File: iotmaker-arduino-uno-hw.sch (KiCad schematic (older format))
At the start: 52 parts, among them J1 BARREL_JACK, J2 USB_A, J3 header Analog, J4 Header I2C, J5 Header module, J6 CONN_02X03, Q1 SI2301DS_GSD, SW1 RESET, SW2 SW_PUSH, U1 CH340G, U2 ATMEGA328P-AU, U3 LM358, U4 FAN1117A-3.3v, U5 FAN1117A-5.0v, Y1 16MHz_GND24, Y2 12MHz_GND24

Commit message: basic completed pcb
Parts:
- added J7: Header Analog, Pin_Headers:Pin_Header_Straight_1x05_Pitch2.54mm, symbol CONN_01X05
- added J8: DHT, Pin_Headers:Pin_Header_Straight_1x03_Pitch2.54mm, symbol CONN_01X03
- J3: value header Analog -> Servo
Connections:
- net +5V: now also J7.1 (P1), J7.4 (P4), J8.1 (P1)
- net ADC6: now also J5.4 (P4); no longer J3.3 (P3)
- net ADC7: now also J7.3 (P3); no longer J5.4 (P4)
- net GND: now also J7.2 (P2), J7.5 (P5), J8.3 (P3)
- net PB1: now also J3.3 (P3)
- net PD2: now also J8.2 (P2); no longer J5.3 (P3)
- net PD4: now also J5.3 (P3)
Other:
- moved on the sheet: J3, J4, J5

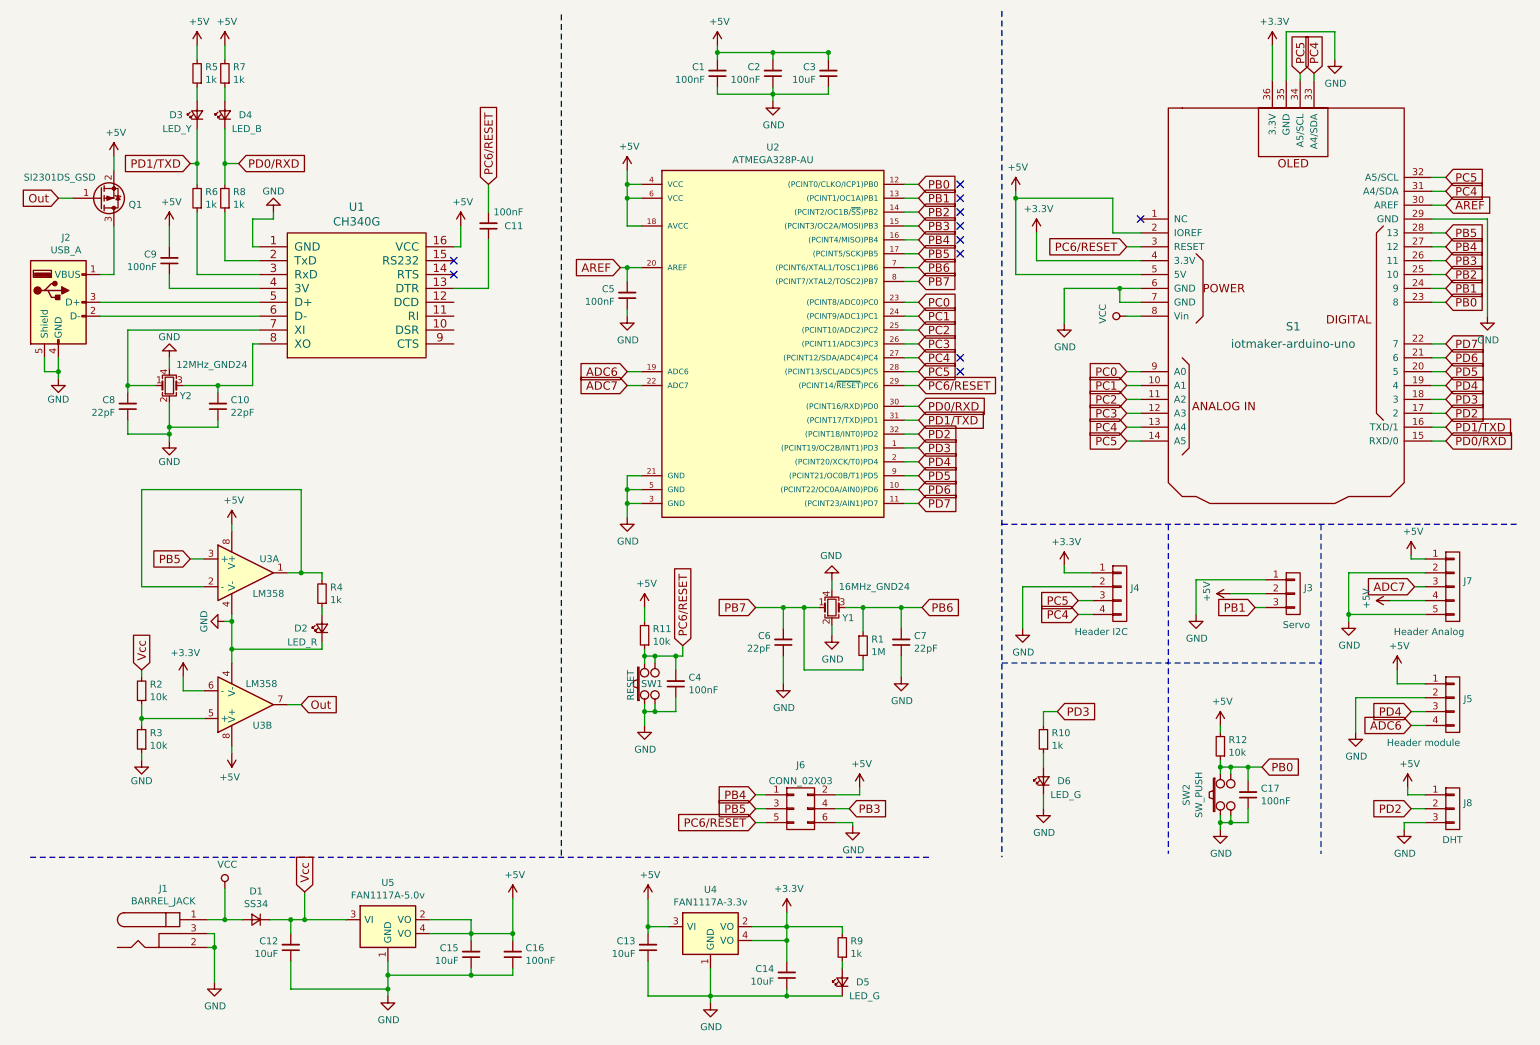
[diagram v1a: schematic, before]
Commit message: cchange CH340G to CH340E & update information board, gerber file
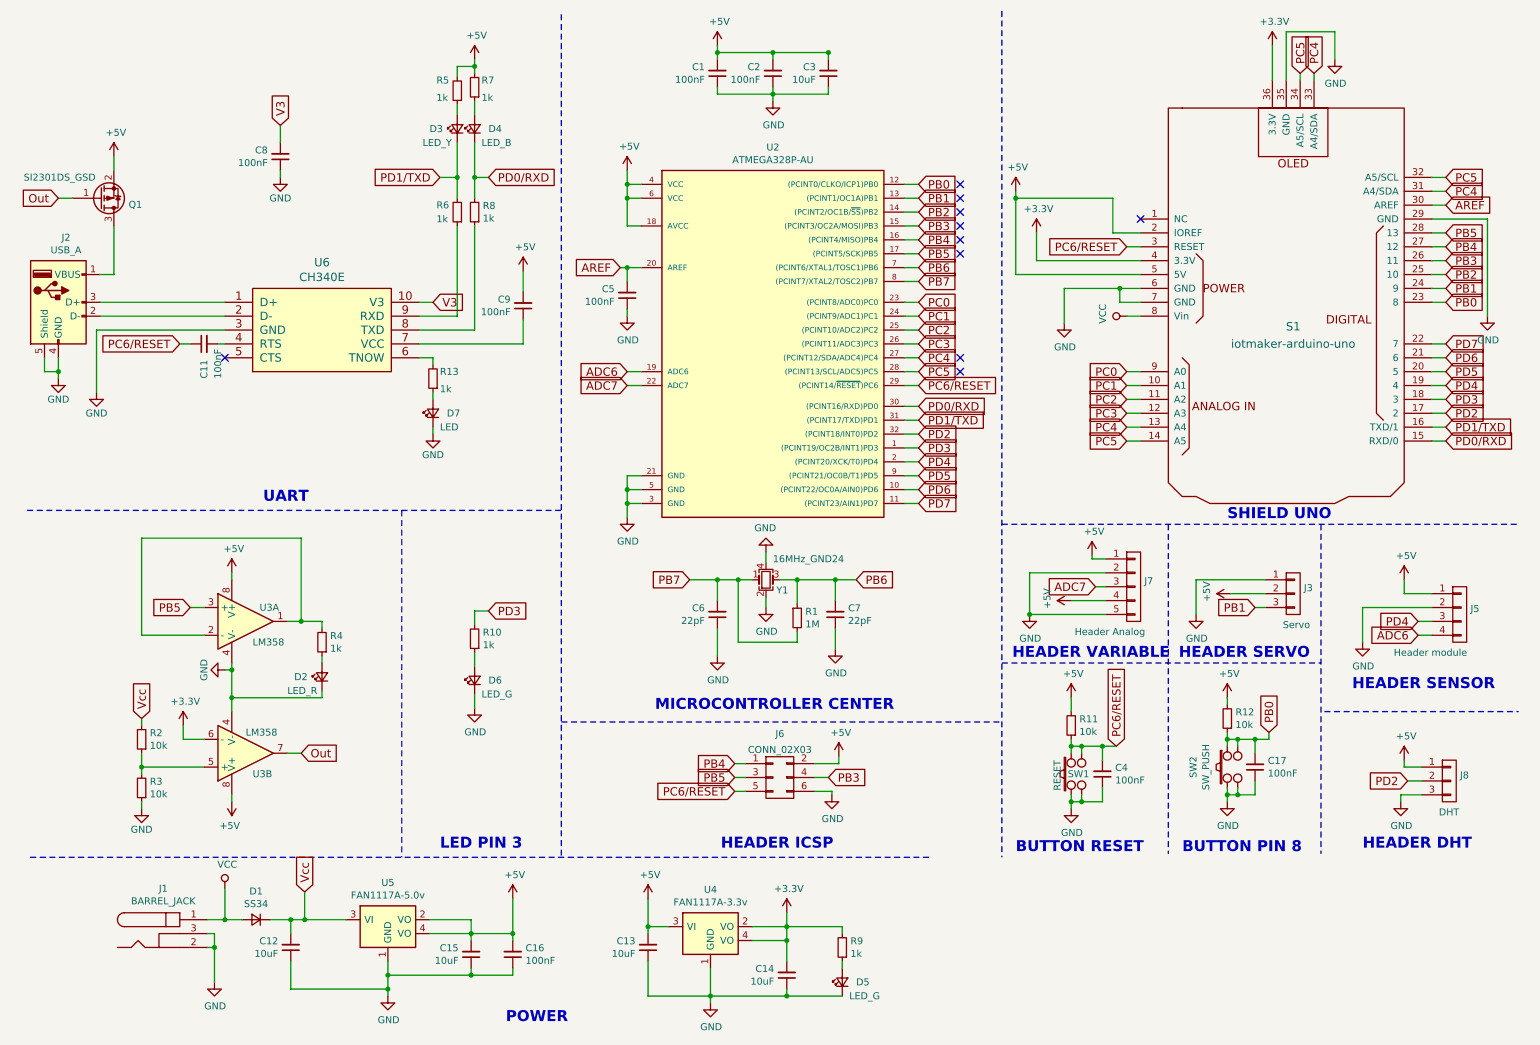
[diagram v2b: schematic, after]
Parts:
- removed C10: 22pF, footprint:C_0603, symbol C_Small
- removed J4: Header I2C, Pin_Headers:Pin_Header_Straight_1x04_Pitch2.54mm, symbol CONN_01X04
- removed U1: CH340G, Housings_SOIC:SOIC-16_3.9x9.9mm_Pitch1.27mm, symbol CH340G
- removed Y2: 12MHz_GND24, Crystals:Crystal_SMD_3225-4pin_3.2x2.5mm_HandSoldering, symbol Crystal_GND24_Small
- added D7: LED, LEDs:LED_0603, symbol LED_Small
- added R13: 1k, footprint:R_0603, symbol R_Small
- added U6: CH340E, Housings_SSOP:MSOP-10_3x3mm_Pitch0.5mm, symbol CH340E
- C8: value 22pF -> 100nF
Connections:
- net GND: now also D7.1 (K), U6.3 (GND)
- net PC6/RESET: now also C11.1; no longer C11.2
- net at R8.1: now also U6.8 (TXD)
- net at R6.1: now also U6.9 (RXD)
- net at C9.1: now also U6.7 (VCC)
- net at J2.3 (D+): now also U6.1 (D+)
- net at J2.2 (D-): now also U6.2 (D-)
- net V3: now reaches C8.2
- net V3: now also U6.10 (V3)
- new net: C11.2, U6.4 (RTS)
- new net: R13.2, U6.6 (TNOW)
- new net: D7.2 (A), R13.1
- no-connect marks 11 -> 10
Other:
- note added: "BUTTON PIN 8"
- note added: "BUTTON RESET"
- note added: "HEADER DHT"
- note added: "HEADER ICSP"
- note added: "HEADER SENSOR"
- note added: "HEADER SERVO"
- note added: "HEADER VARIABLE"
- note added: "LED PIN 3"
- note added: "MICROCONTROLLER CENTER"
- note added: "POWER"
- note added: "SHIELD UNO"
- note added: "UART"
- moved on the sheet: C11, C17, C4, C6, C7, C9, D2, D3, D4, D6, J5, J6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

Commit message: drop c4
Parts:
- removed C4: 100nF, footprint:C_0603, symbol C_Small
- C1, C11, C12, C13, C14, C15, C16, C17, C2, C3, C5, C6, C7, C8, C9: symbol C_Small -> iotmaker-arduino-uno-hw-rescue:C_Small-RESCUE-iotmaker-arduino-uno-hw
- D1: symbol D_Small -> iotmaker-arduino-uno-hw-rescue:D_Small-RESCUE-iotmaker-arduino-uno-hw
- D2, D3, D4, D5, D6, D7: symbol LED_Small -> iotmaker-arduino-uno-hw-rescue:LED_Small-RESCUE-iotmaker-arduino-uno-hw
- J1: symbol BARREL_JACK -> iotmaker-arduino-uno-hw-rescue:BARREL_JACK-RESCUE-iotmaker-arduino-uno-hw
- J2: symbol USB_A -> iotmaker-arduino-uno-hw-rescue:USB_A-RESCUE-iotmaker-arduino-uno-hw
- J3, J8: symbol CONN_01X03 -> iotmaker-arduino-uno-hw-rescue:CONN_01X03-RESCUE-iotmaker-arduino-uno-hw
- J5: symbol CONN_01X04 -> iotmaker-arduino-uno-hw-rescue:CONN_01X04-RESCUE-iotmaker-arduino-uno-hw
- J6: symbol CONN_02X03 -> iotmaker-arduino-uno-hw-rescue:CONN_02X03-RESCUE-iotmaker-arduino-uno-hw
- J7: symbol CONN_01X05 -> iotmaker-arduino-uno-hw-rescue:CONN_01X05-RESCUE-iotmaker-arduino-uno-hw
- Q1: symbol Q_PMOS_GSD -> iotmaker-arduino-uno-hw-rescue:Q_PMOS_GSD-RESCUE-iotmaker-arduino-uno-hw
- R1, R10, R11, R12, R13, R2, R3, R4, R5, R6, R7, R8, R9: symbol R_Small -> iotmaker-arduino-uno-hw-rescue:R_Small-RESCUE-iotmaker-arduino-uno-hw
- S1: symbol iotmaker-arduino-uno -> iotmaker-arduino-uno-hw-rescue:iotmaker-arduino-uno-RESCUE-iotmaker-arduino-uno-hw
- SW1, SW2: symbol SW_PUSH -> iotmaker-arduino-uno-hw-rescue:SW_PUSH-RESCUE-iotmaker-arduino-uno-hw
- U2: symbol ATMEGA328P-AU -> iotmaker-arduino-uno-hw-rescue:ATMEGA328P-AU-RESCUE-iotmaker-arduino-uno-hw
- U3: symbol LM358 -> iotmaker-arduino-uno-hw-rescue:LM358-RESCUE-iotmaker-arduino-uno-hw
- U4, U5: symbol NCP1117DT285G_MountingTab -> iotmaker-arduino-uno-hw-rescue:NCP1117DT285G_MountingTab-RESCUE-iotmaker-arduino-uno-hw
- U6: symbol CH340E -> iotmaker-arduino-uno-hw-rescue:CH340E-RESCUE-iotmaker-arduino-uno-hw
- Y1: footprint Crystals:Crystal_SMD_3225-4pin_3.2x2.5mm_HandSoldering -> Crystals:Crystal_SMD_3225-4pin_3.2x2.5mm; symbol Crystal_GND24_Small -> iotmaker-arduino-uno-hw-rescue:Crystal_GND24_Small-RESCUE-iotmaker-arduino-uno-hw

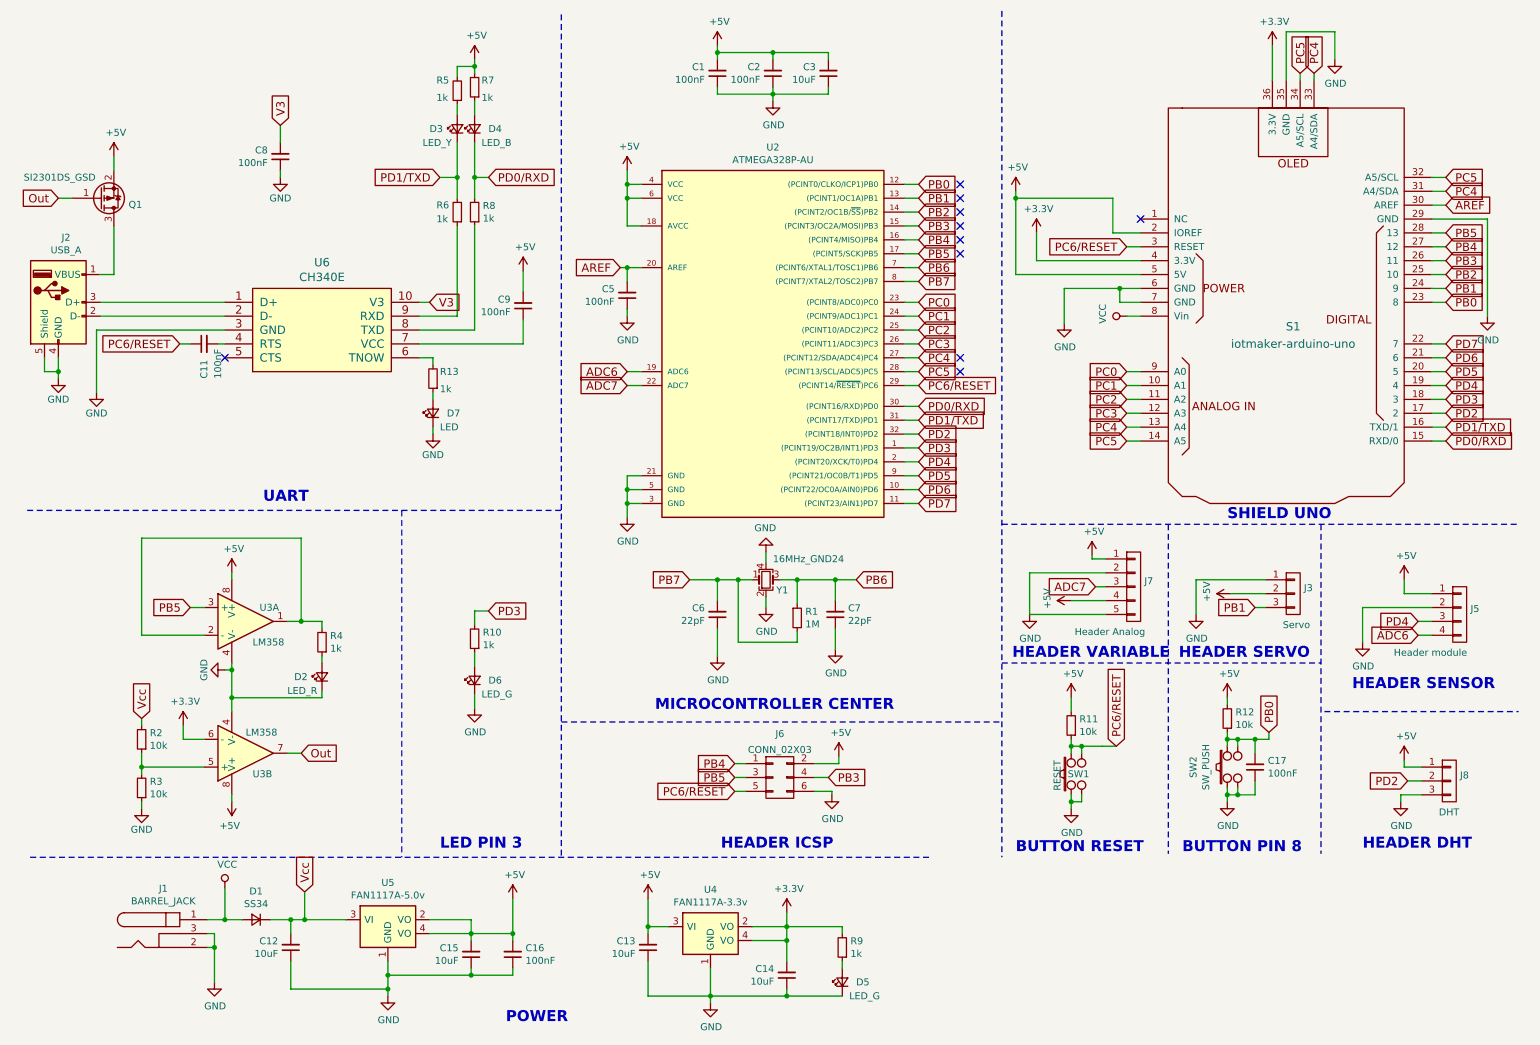
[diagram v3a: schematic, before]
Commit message: change button pin8 to pin2 and header pin2 to pin7
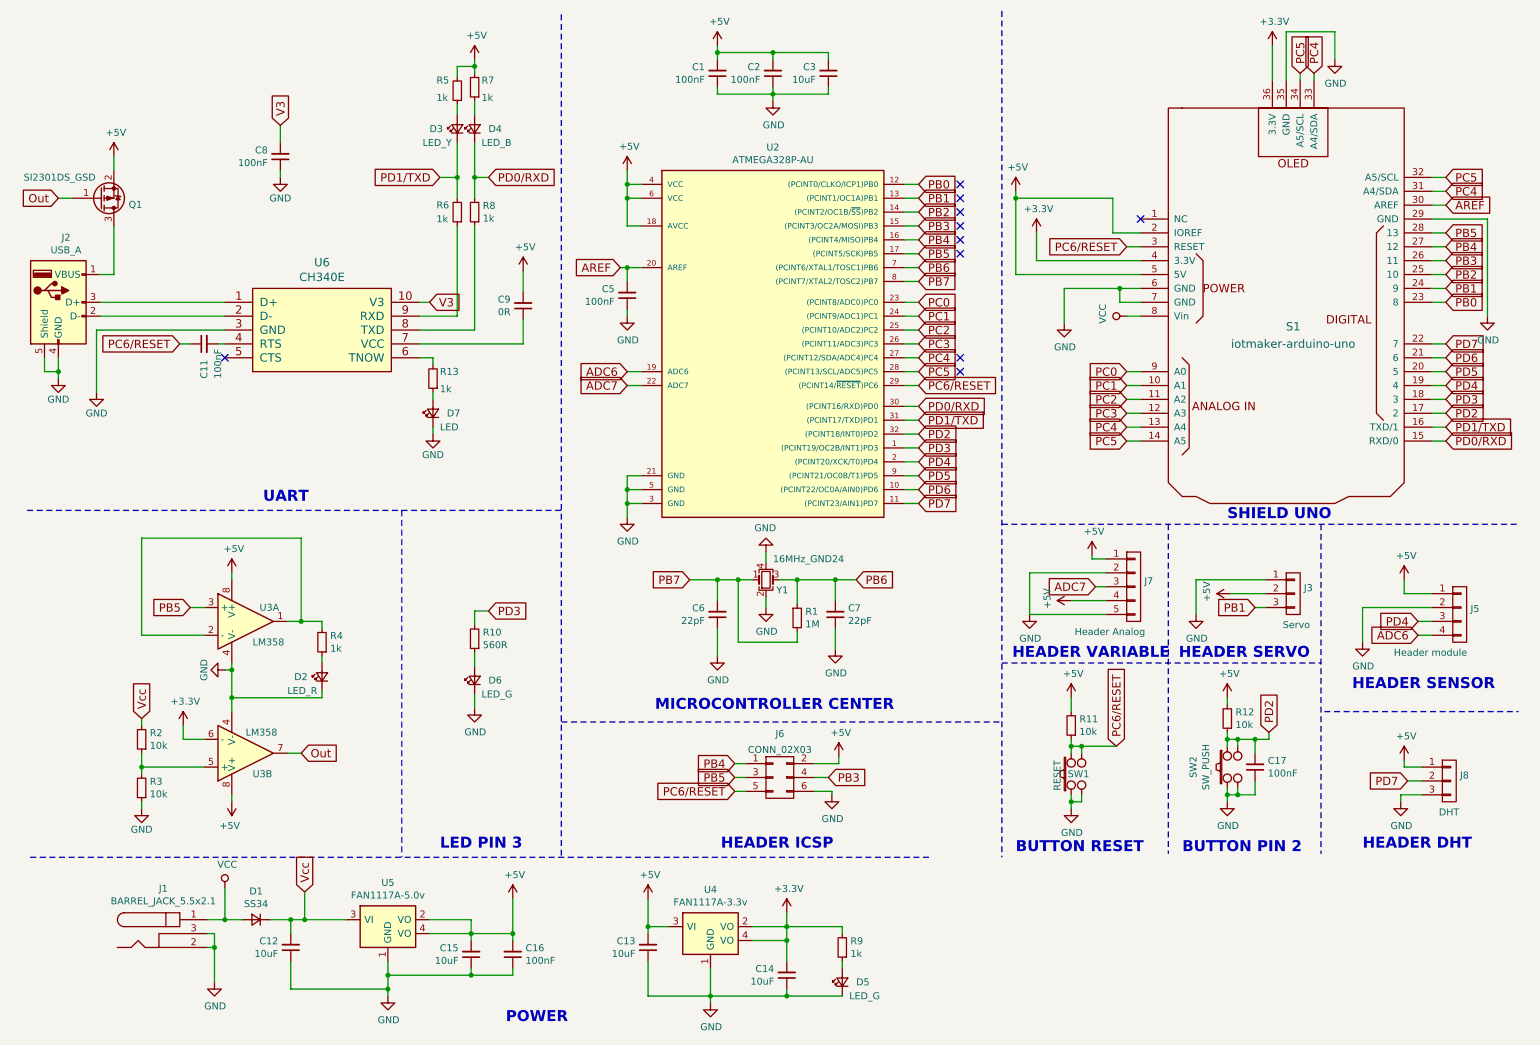
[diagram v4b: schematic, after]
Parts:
- C9: value 100nF -> 0R
- J1: value BARREL_JACK -> BARREL_JACK_5.5x2.1
- R10: value 1k -> 560R
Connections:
- net PB0: no longer C17.2, R12.1, SW2.1, SW2.2
- net PD2: now also C17.2, R12.1, SW2.1, SW2.2; no longer J8.2 (P2)
- net PD7: now also J8.2 (P2)
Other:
- note added: "BUTTON PIN 2"
- note removed: "BUTTON PIN 8"
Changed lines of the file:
@@
 P 4050 2575
 F 0 "C9" H 3959 2529 50  0000 R CNN
-F 1 "100nF" H 3959 2620 50  0000 R CNN
+F 1 "0R" H 3959 2620 50  0000 R CNN
 F 2 "footprint:C_0603" H 4050 2575 50  0001 C CNN
 F 3 "" H 4050 2575 50  0001 C CNN
@@
 P 1475 7100
 F 0 "J1" H 1456 7425 50  0000 C CNN
-F 1 "BARREL_JACK" H 1456 7334 50  0000 C CNN
+F 1 "BARREL_JACK_5.5x2.1" H 1456 7334 50  0000 C CNN
 F 2 "footprint:BARREL_JACK" H 1475 7100 50  0001 C CNN
 F 3 "" H 1475 7100 50  0001 C CNN
@@
 P 3700 4975
 F 0 "R10" H 3641 4929 50  0000 R CNN
-F 1 "1k" H 3641 5020 50  0000 R CNN
+F 1 "560R" H 3641 5020 50  0000 R CNN
 F 2 "footprint:R_0603" H 3700 4975 50  0001 C CNN
 F 3 "" H 3700 4975 50  0001 C CNN
@@
 Wire Wire Line
 	8000 5750 8075 5750
-Wire Wire Line
-	8075 5750 8225 5750
-Wire Wire Line
-	8225 5750 8325 5750
 Connection ~ 8000 5750
 $Comp
@@
 Text GLabel 5575 6075 0    60   Input ~ 0
 PC6/RESET
-Text GLabel 9425 5650 1    60   Input ~ 0
-PB0
 $Comp
 L iotmaker-arduino-uno-hw-rescue:CONN_01X05-RESCUE-iotmaker-arduino-uno-hw J7
@@
 Wire Wire Line
 	10375 6100 10375 6150
-Text GLabel 10425 6000 0    60   Input ~ 0
-PD2
 Wire Wire Line
 	10425 6000 10525 6000
@@
 BUTTON RESET
 Text Notes 8800 6525 0    79   ~ 16
-BUTTON PIN 8
+BUTTON PIN 2
 Text Notes 10100 6500 0    79   ~ 16
 HEADER DHT
@@
 Text Notes 3925 7750 0    79   ~ 16
 POWER
+Text GLabel 9425 5650 1    60   Input ~ 0
+PD2
+Text GLabel 10425 6000 0    60   Input ~ 0
+PD7
+Wire Wire Line
+	8075 5750 8325 5750
 $EndSCHEMATC
